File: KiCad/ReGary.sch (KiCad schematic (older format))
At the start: 10 parts, among them U4 SN74CBT16210, U5 SN74CBT16210, U6 SN74CBT16210, U7 SN74CBT16210, U8 PLCC_84_plug, U9 PLCC_84_plug

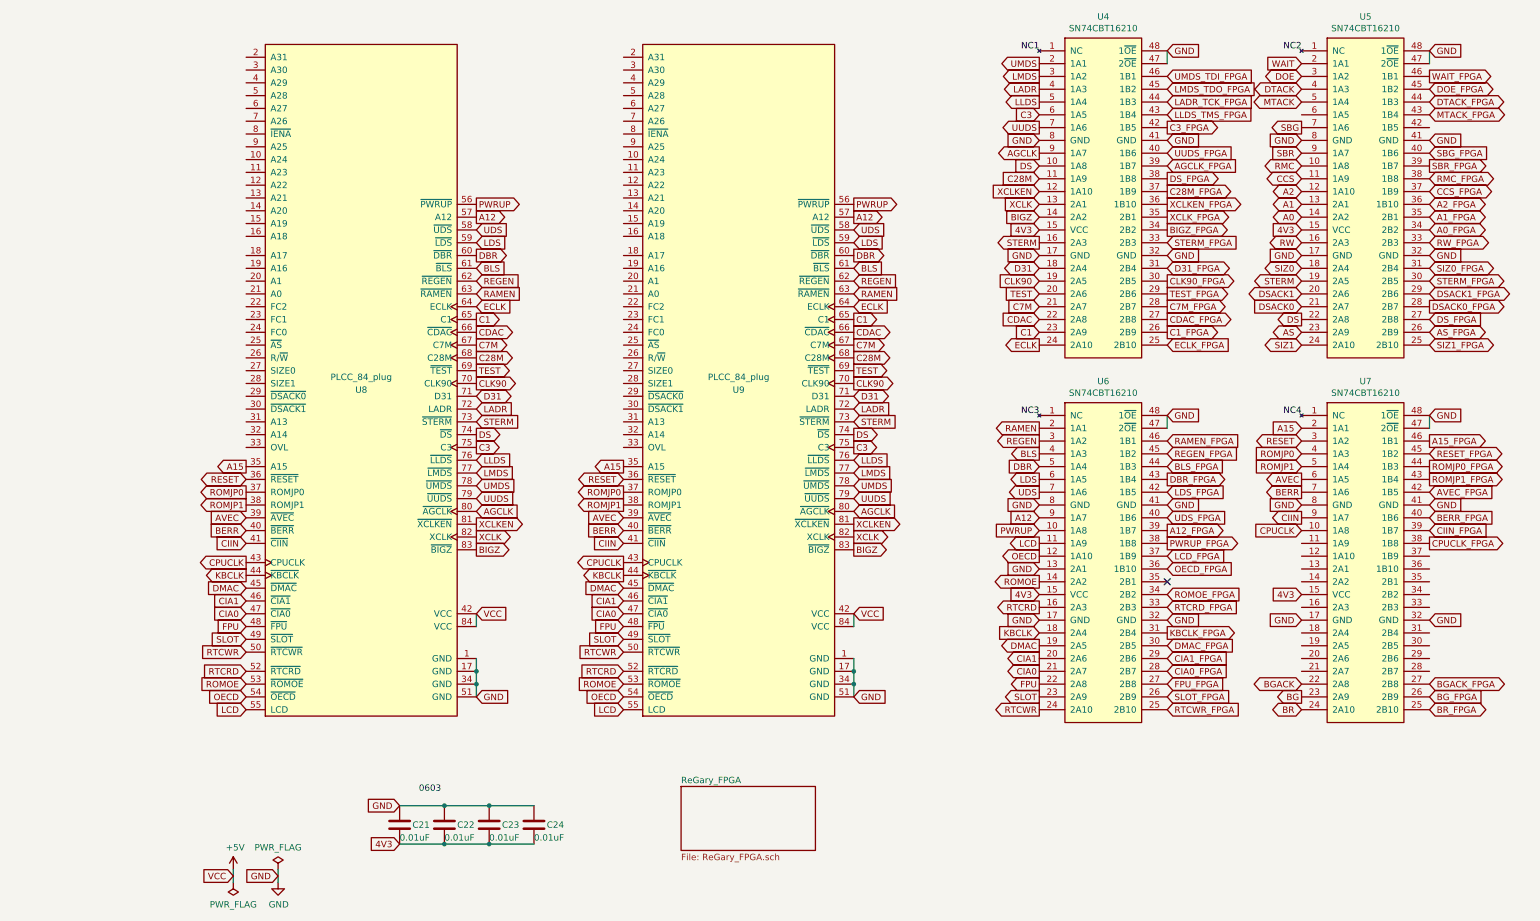
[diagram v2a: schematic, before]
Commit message: More pin assignments and routing
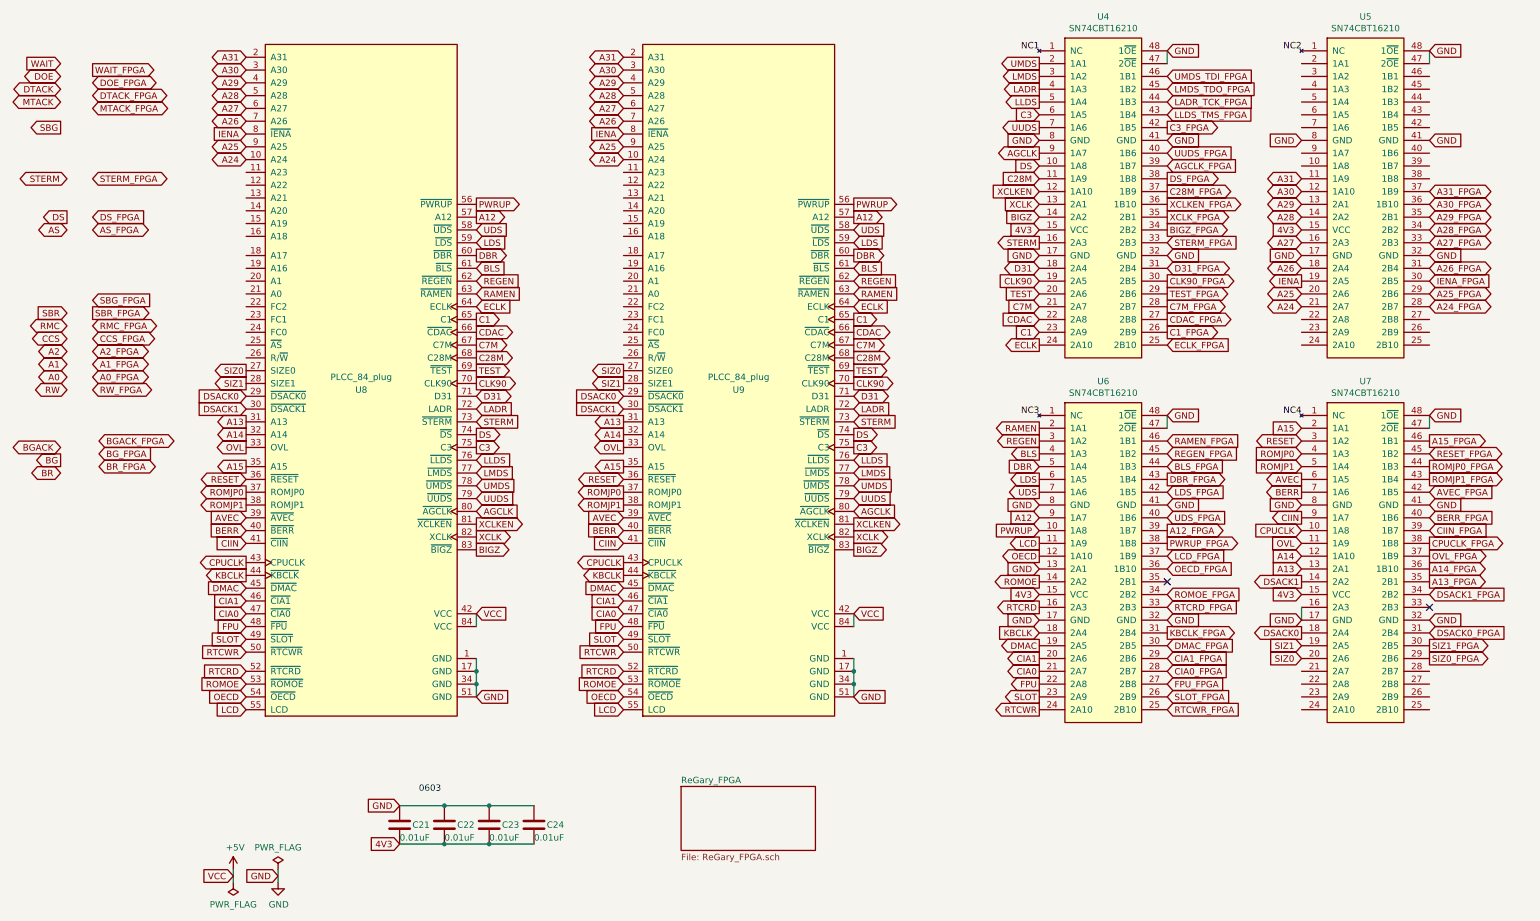
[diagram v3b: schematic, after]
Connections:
- net A0: no longer U5.14 (2A2)
- net A0_FPGA: no longer U5.34 (2B2)
- net A1: no longer U5.13 (2A1)
- net A1_FPGA: no longer U5.35 (2B1)
- net A2: no longer U5.12 (1A10)
- net A2_FPGA: no longer U5.36 (1B10)
- net AS: no longer U5.23 (2A9)
- net AS_FPGA: no longer U5.26 (2B9)
- net BG: no longer U7.23 (2A9)
- net BGACK: no longer U7.22 (2A8)
- net BGACK_FPGA: no longer U7.27 (2B8)
- net BG_FPGA: no longer U7.26 (2B9)
- net BR: no longer U7.24 (2A10)
- net BR_FPGA: no longer U7.25 (2B10)
- net CCS: no longer U5.11 (1A9)
- net CCS_FPGA: no longer U5.37 (1B9)
- net DOE: no longer U5.3 (1A2)
- net DOE_FPGA: no longer U5.45 (1B2)
- net DS: no longer U5.22 (2A8)
- net DSACK0: now also U7.18 (2A4), U8.29 (~DSACK0), U9.29 (~DSACK0); no longer U5.21 (2A7)
- net DSACK0_FPGA: now also U7.31 (2B4); no longer U5.28 (2B7)
- net DSACK1: now also U7.14 (2A2), U8.30 (~DSACK1), U9.30 (~DSACK1); no longer U5.20 (2A6)
- net DSACK1_FPGA: now also U7.34 (2B2); no longer U5.29 (2B6)
- net DS_FPGA: no longer U5.27 (2B8)
- net DTACK: no longer U5.4 (1A3)
- net DTACK_FPGA: no longer U5.44 (1B3)
- net GND: now also U7.16 (2A3)
- net MTACK: no longer U5.5 (1A4)
- net MTACK_FPGA: no longer U5.43 (1B4)
- net RMC: no longer U5.10 (1A8)
- net RMC_FPGA: no longer U5.38 (1B8)
- net RW: no longer U5.16 (2A3)
- net RW_FPGA: no longer U5.33 (2B3)
- net SBG: no longer U5.7 (1A6)
- net SBG_FPGA: no longer U5.40 (1B6)
- net SBR: no longer U5.9 (1A7)
- net SBR_FPGA: no longer U5.39 (1B7)
- net SIZ0: now also U7.20 (2A6), U8.27 (SIZE0), U9.27 (SIZE0); no longer U5.18 (2A4)
- net SIZ0_FPGA: now also U7.29 (2B6); no longer U5.31 (2B4)
- net SIZ1: now also U7.19 (2A5), U8.28 (SIZE1), U9.28 (SIZE1); no longer U5.24 (2A10)
- net SIZ1_FPGA: now also U7.30 (2B5); no longer U5.25 (2B10)
- net STERM: no longer U5.19 (2A5)
- net STERM_FPGA: no longer U5.30 (2B5)
- net WAIT: no longer U5.2 (1A1)
- net WAIT_FPGA: no longer U5.46 (1B1)
- net OVL: now reaches U7.11 (1A9)
- net OVL: now also U8.33 (OVL), U9.33 (OVL)
- net A14: now reaches U7.12 (1A10)
- net A14: now also U8.32 (A14), U9.32 (A14)
- net A13: now reaches U7.13 (2A1)
- net A13: now also U8.31 (A13), U9.31 (A13)
- net A13_FPGA: now reaches U7.35 (2B1)
- net A14_FPGA: now reaches U7.36 (1B10)
- net OVL_FPGA: now reaches U7.37 (1B9)
- net A24: now reaches U9.10 (A24)
- net A24: now also U5.21 (2A7), U8.10 (A24)
- net A31: now reaches U9.2 (A31)
- net A31: now also U5.11 (1A9), U8.2 (A31)
- net A30: now reaches U9.3 (A30)
- net A30: now also U5.12 (1A10), U8.3 (A30)
- net A29: now reaches U9.4 (A29)
- net A29: now also U5.13 (2A1), U8.4 (A29)
- net A28: now reaches U9.5 (A28)
- net A28: now also U5.14 (2A2), U8.5 (A28)
- net A27: now reaches U9.6 (A27)
- net A27: now also U5.16 (2A3), U8.6 (A27)
- net A26: now reaches U9.7 (A26)
- net A26: now also U5.18 (2A4), U8.7 (A26)
- net IENA: now reaches U9.8 (~IENA)
- net IENA: now also U5.19 (2A5), U8.8 (~IENA)
- net A25: now reaches U9.9 (A25)
- net A25: now also U5.20 (2A6), U8.9 (A25)
- new net A24_FPGA: U5.28 (2B7)
- new net A25_FPGA: U5.29 (2B6)
- new net A26_FPGA: U5.31 (2B4)
- new net A27_FPGA: U5.33 (2B3)
- new net A28_FPGA: U5.34 (2B2)
- new net A29_FPGA: U5.35 (2B1)
- new net A30_FPGA: U5.36 (1B10)
- new net A31_FPGA: U5.37 (1B9)
- new net IENA_FPGA: U5.30 (2B5)
- no-connect marks 1 -> 2
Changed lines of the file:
@@
 Text GLabel 7150 4500 0    50   Input ~ 0
 GND
-Text GLabel 10200 3250 2    50   BiDi ~ 0
+Text GLabel 10200 5600 2    50   Output ~ 0
 SIZ1_FPGA
 Text GLabel 8150 1750 2    50   Input ~ 0
@@
 Text GLabel 8150 1950 2    50   Output ~ 0
 DS_FPGA
-Text GLabel 10200 1150 2    50   Output ~ 0
+Text GLabel -250 1100 2    50   Output ~ 0
 WAIT_FPGA
-Text GLabel 10200 1250 2    50   BiDi ~ 0
+Text GLabel -250 1200 2    50   BiDi ~ 0
 DOE_FPGA
-Text GLabel 10200 1350 2    50   BiDi ~ 0
+Text GLabel -250 1300 2    50   BiDi ~ 0
 DTACK_FPGA
-Text GLabel 10200 1450 2    50   BiDi ~ 0
+Text GLabel -250 1400 2    50   BiDi ~ 0
 MTACK_FPGA
-Text GLabel 10200 1850 2    50   Output ~ 0
+Text GLabel -250 3000 2    50   Output ~ 0
 SBR_FPGA
-Text GLabel 10200 1950 2    50   BiDi ~ 0
+Text GLabel -250 3100 2    50   BiDi ~ 0
 RMC_FPGA
-Text GLabel 10200 2050 2    50   BiDi ~ 0
+Text GLabel -250 3200 2    50   BiDi ~ 0
 CCS_FPGA
-Text GLabel 10200 2150 2    50   BiDi ~ 0
+Text GLabel -250 3300 2    50   BiDi ~ 0
 A2_FPGA
-Text GLabel 10200 2250 2    50   BiDi ~ 0
+Text GLabel -250 3400 2    50   BiDi ~ 0
 A1_FPGA
-Text GLabel 10200 1750 2    50   Input ~ 0
+Text GLabel -250 2900 2    50   Input ~ 0
 SBG_FPGA
-Text GLabel 10200 2450 2    50   BiDi ~ 0
+Text GLabel -250 3600 2    50   BiDi ~ 0
 RW_FPGA
-Text GLabel 10200 2650 2    50   BiDi ~ 0
+Text GLabel 10200 5700 2    50   Output ~ 0
 SIZ0_FPGA
-Text GLabel 10200 2750 2    50   BiDi ~ 0
+Text GLabel -250 1950 2    50   BiDi ~ 0
 STERM_FPGA
-Text GLabel 10200 3050 2    50   Input ~ 0
+Text GLabel -250 2250 2    50   Input ~ 0
 DS_FPGA
-Text GLabel 10200 3150 2    50   BiDi ~ 0
+Text GLabel -250 2350 2    50   BiDi ~ 0
 AS_FPGA
 Text GLabel 8150 4000 2    50   Input ~ 0
@@
 Text GLabel 10200 4800 2    50   Output ~ 0
 CPUCLK_FPGA
-Text GLabel 10200 5900 2    50   BiDi ~ 0
+Text GLabel -200 4000 2    50   BiDi ~ 0
 BGACK_FPGA
-Text GLabel 10200 6000 2    50   Input ~ 0
+Text GLabel -200 4100 2    50   Input ~ 0
 BG_FPGA
-Text GLabel 10200 6100 2    50   BiDi ~ 0
+Text GLabel -200 4200 2    50   BiDi ~ 0
 BR_FPGA
 Wire Wire Line
@@
 Text GLabel 8150 2250 2    50   Output ~ 0
 XCLK_FPGA
-Text GLabel 9200 1950 0    50   BiDi ~ 0
+Text GLabel -450 3200 0    50   BiDi ~ 0
 CCS
-Text GLabel 9200 2050 0    50   BiDi ~ 0
+Text GLabel -450 3300 0    50   BiDi ~ 0
 A2
-Text GLabel 9200 2150 0    50   BiDi ~ 0
+Text GLabel -450 3400 0    50   BiDi ~ 0
 A1
-Text GLabel 9200 2250 0    50   BiDi ~ 0
+Text GLabel -450 3500 0    50   BiDi ~ 0
 A0
-Text GLabel 9200 2450 0    50   BiDi ~ 0
+Text GLabel -450 3600 0    50   BiDi ~ 0
 RW
-Text GLabel 9200 2650 0    50   BiDi ~ 0
+Text GLabel 950  3450 0    50   Output ~ 0
 SIZ0
-Text GLabel 9200 3250 0    50   BiDi ~ 0
+Text GLabel 950  3550 0    50   Output ~ 0
 SIZ1
-Text GLabel 9200 3150 0    50   BiDi ~ 0
+Text GLabel -450 2350 0    50   BiDi ~ 0
 AS
-Text GLabel 9200 3050 0    50   Output ~ 0
+Text GLabel -450 2250 0    50   Output ~ 0
 DS
-Text GLabel 9200 2950 0    50   Input ~ 0
+Text GLabel 950  3650 0    50   Input ~ 0
 DSACK0
-Text GLabel 9200 2850 0    50   BiDi ~ 0
+Text GLabel 950  3750 0    50   Input ~ 0
 DSACK1
-Text GLabel 9200 2750 0    50   BiDi ~ 0
+Text GLabel -450 1950 0    50   BiDi ~ 0
 STERM
-Text GLabel 9200 1850 0    50   BiDi ~ 0
+Text GLabel -450 3100 0    50   BiDi ~ 0
 RMC
-Text GLabel 9200 1750 0    50   Input ~ 0
+Text GLabel -450 3000 0    50   Input ~ 0
 SBR
-Text GLabel 9200 1550 0    50   Output ~ 0
+Text GLabel -500 1550 0    50   Output ~ 0
 SBG
-Text GLabel 9200 1350 0    50   BiDi ~ 0
+Text GLabel -500 1350 0    50   BiDi ~ 0
 MTACK
-Text GLabel 9200 1250 0    50   BiDi ~ 0
+Text GLabel -500 1250 0    50   BiDi ~ 0
 DTACK
-Text GLabel 9200 1150 0    50   BiDi ~ 0
+Text GLabel -500 1150 0    50   BiDi ~ 0
 DOE
-Text GLabel 9200 1050 0    50   Input ~ 0
+Text GLabel -500 1050 0    50   Input ~ 0
 WAIT
-Text GLabel 9200 6100 0    50   BiDi ~ 0
+Text GLabel -500 4250 0    50   BiDi ~ 0
 BR
-Text GLabel 9200 6000 0    50   Output ~ 0
+Text GLabel -500 4150 0    50   Output ~ 0
 BG
-Text GLabel 9200 5900 0    50   BiDi ~ 0
+Text GLabel -500 4050 0    50   BiDi ~ 0
 BGACK
 Text GLabel 2750 2450 2    50   Input ~ 0
@@
 Text GLabel 8150 1550 2    50   Output ~ 0
 C3_FPGA
-Text GLabel 10200 2350 2    50   BiDi ~ 0
+Text GLabel -250 3500 2    50   BiDi ~ 0
 A0_FPGA
-Text GLabel 10200 2850 2    50   BiDi ~ 0
+Text GLabel 10200 5200 2    50   Input ~ 0
 DSACK1_FPGA
-Text GLabel 10200 2950 2    50   Output ~ 0
+Text GLabel 10200 5500 2    50   Input ~ 0
 DSACK0_FPGA
 $Sheet
@@
 Text GLabel 10200 4000 2    50   Output ~ 0
 A15_FPGA
+Text GLabel 950  3850 0    50   Output ~ 0
+A13
+Text GLabel 950  3950 0    50   Output ~ 0
+A14
+Text GLabel 950  4050 0    50   Output ~ 0
+OVL
+Text GLabel 3900 3850 0    50   Output ~ 0
+A13
+Text GLabel 3900 3950 0    50   Output ~ 0
+A14
+Text GLabel 3900 4050 0    50   Output ~ 0
+OVL
+Text GLabel 9200 4900 0    50   Input ~ 0
+A14
+Text GLabel 9200 4800 0    50   Input ~ 0
+OVL
+Text GLabel 9200 5000 0    50   Input ~ 0
+A13
+Text GLabel 10200 5000 2    50   Output ~ 0
+A14_FPGA
+Text GLabel 10200 4900 2    50   Output ~ 0
+OVL_FPGA
+Text GLabel 10200 5100 2    50   Output ~ 0
+A13_FPGA
+Text GLabel 950  1000 0    50   BiDi ~ 0
+A31
+Text GLabel 950  1100 0    50   BiDi ~ 0
+A30
+Text GLabel 950  1200 0    50   BiDi ~ 0
+A29
+Text GLabel 950  1300 0    50   BiDi ~ 0
+A28
+Text GLabel 950  1400 0    50   BiDi ~ 0
+A27
+Text GLabel 950  1500 0    50   BiDi ~ 0
+A26
+Text GLabel 950  1600 0    50   Input ~ 0
+IENA
+Text GLabel 950  1700 0    50   BiDi ~ 0
+A25
+Text GLabel 950  1800 0    50   BiDi ~ 0
+A24
+Text GLabel 3900 1000 0    50   BiDi ~ 0
+A31
+Text GLabel 3900 1100 0    50   BiDi ~ 0
+A30
+Text GLabel 3900 1200 0    50   BiDi ~ 0
+A29
+Text GLabel 3900 1300 0    50   BiDi ~ 0
+A28
+Text GLabel 3900 1400 0    50   BiDi ~ 0
+A27
+Text GLabel 3900 1500 0    50   BiDi ~ 0
+A26
+Text GLabel 3900 1600 0    50   Input ~ 0
+IENA
+Text GLabel 3900 1700 0    50   BiDi ~ 0
+A25
+Text GLabel 3900 1800 0    50   BiDi ~ 0
+A24
+Text GLabel 9200 1950 0    50   BiDi ~ 0
+A31
+Text GLabel 9200 2050 0    50   BiDi ~ 0
+A30
+Text GLabel 9200 2150 0    50   BiDi ~ 0
+A29
+Text GLabel 9200 2250 0    50   BiDi ~ 0
+A28
+Text GLabel 9200 2450 0    50   BiDi ~ 0
+A27
+Text GLabel 9200 2650 0    50   BiDi ~ 0
+A26
+Text GLabel 9200 2750 0    50   Output ~ 0
+IENA
+Text GLabel 9200 2850 0    50   BiDi ~ 0
+A25
+Text GLabel 9200 2950 0    50   BiDi ~ 0
+A24
+Text GLabel 10200 2050 2    50   BiDi ~ 0
+A31_FPGA
+Text GLabel 10200 2150 2    50   BiDi ~ 0
+A30_FPGA
+Text GLabel 10200 2250 2    50   BiDi ~ 0
+A29_FPGA
+Text GLabel 10200 2350 2    50   BiDi ~ 0
+A28_FPGA
+Text GLabel 10200 2450 2    50   BiDi ~ 0
+A27_FPGA
+Text GLabel 10200 2650 2    50   BiDi ~ 0
+A26_FPGA
+Text GLabel 10200 2750 2    50   Input ~ 0
+IENA_FPGA
+Text GLabel 10200 2850 2    50   BiDi ~ 0
+A25_FPGA
+Text GLabel 10200 2950 2    50   BiDi ~ 0
+A24_FPGA
+Text GLabel 3900 3650 0    50   Input ~ 0
+DSACK0
+Text GLabel 3900 3750 0    50   Input ~ 0
+DSACK1
+Text GLabel 9200 5500 0    50   Output ~ 0
+DSACK0
+Text GLabel 9200 5100 0    50   Output ~ 0
+DSACK1
+Wire Wire Line
+	9200 5300 9200 5400
+NoConn ~ 10200 5300
+Text GLabel 3900 3450 0    50   Output ~ 0
+SIZ0
+Text GLabel 3900 3550 0    50   Output ~ 0
+SIZ1
+Text GLabel 9200 5700 0    50   Input ~ 0
+SIZ0
+Text GLabel 9200 5600 0    50   Input ~ 0
+SIZ1
 $EndSCHEMATC
